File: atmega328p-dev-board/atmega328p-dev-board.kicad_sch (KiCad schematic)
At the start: 0 parts

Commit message: Completed 5V power supply schematic
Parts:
- added C1, C2: 10u, symbol Device:C_Polarized
- added C3, C4: 0.1u, symbol Device:C
- added D1: LED, symbol Device:LED
- added J2: Barrel_Jack, symbol Connector:Barrel_Jack
- added R1: 330, symbol Device:R
- added U1: LM7805_TO220, Package_TO_SOT_THT:TO-220-3_Vertical, symbol Regulator_Linear:LM7805_TO220
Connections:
- new net: C1.1, C4.1, J2.1, U1.1 (VI)
- new net: D1.2 (A), R1.2
- new net +5V: C2.1, C3.1, R1.1, U1.3 (VO)
- new net GND: C1.2, C2.2, C3.2, C4.2, D1.1 (K), J2.2, U1.2 (GND)

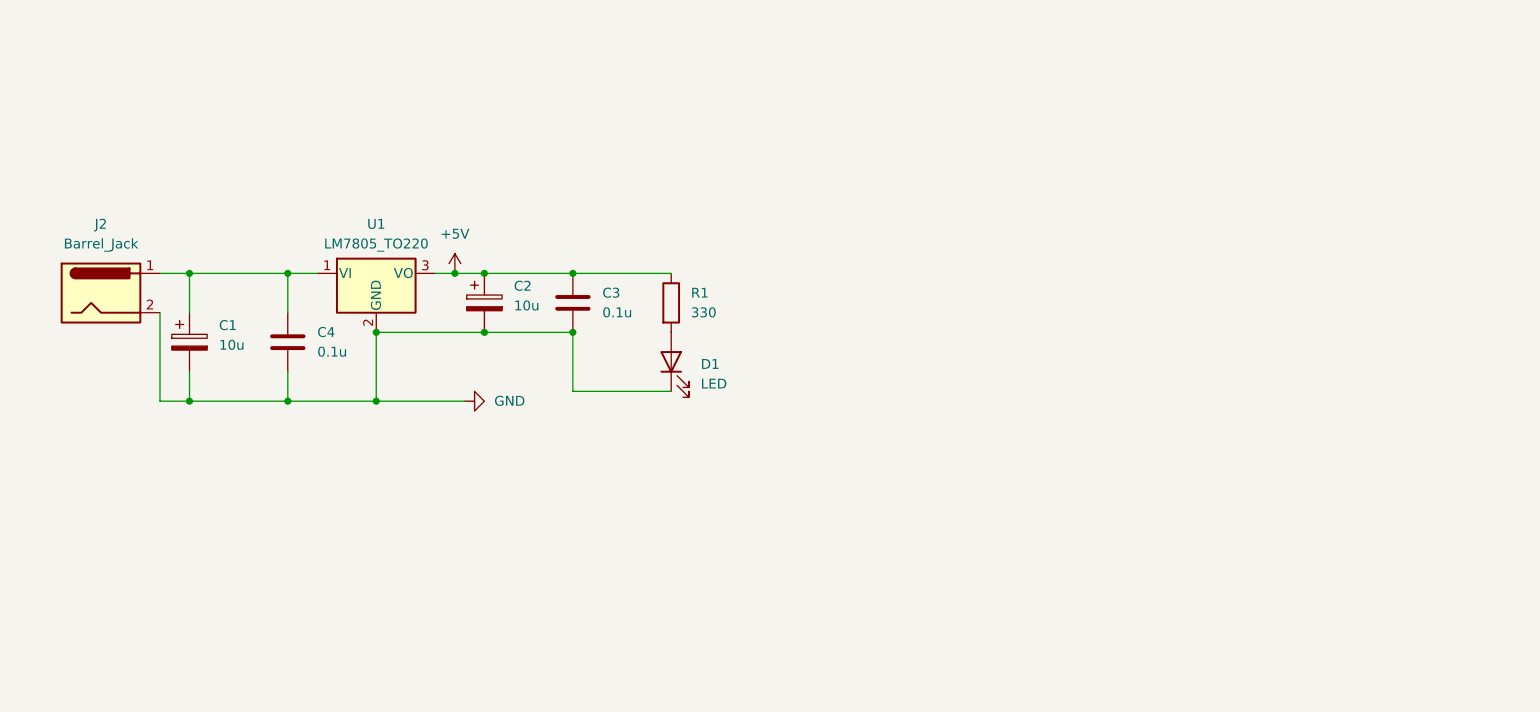
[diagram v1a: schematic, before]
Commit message: Added ATmega328P microcontroller and 16MHz crystal oscillator clock circuit
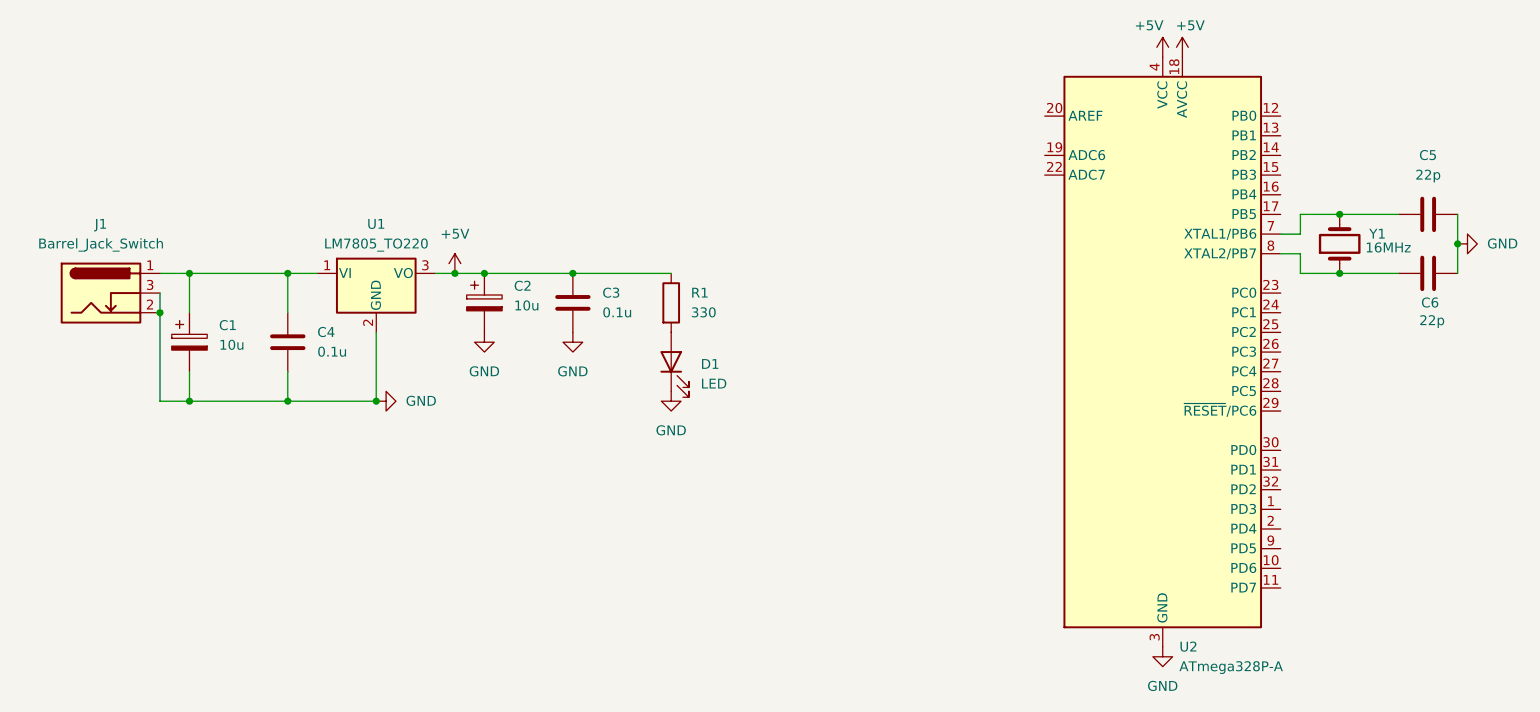
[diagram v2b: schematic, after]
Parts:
- removed J2: Barrel_Jack, symbol Connector:Barrel_Jack
- added C5, C6: 22p, symbol Device:C
- added J1: Barrel_Jack_Switch, symbol Connector:Barrel_Jack_Switch
- added U2: ATmega328P-A, Package_QFP:TQFP-32_7x7mm_P0.8mm, symbol MCU_Microchip_ATmega:ATmega328P-A
- added Y1: 16MHz, symbol Device:Crystal
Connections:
- net +5V: now also U2.18 (AVCC), U2.4 (VCC), U2.6 (VCC)
- net GND: now also C5.2, C6.2, J1.2, J1.3, U2.21 (GND), U2.3 (GND), U2.5 (GND)
- net at C1.1, C4.1, U1.1 (VI): now also J1.1
- new net: C6.1, U2.8 (XTAL2/PB7), Y1.1
- new net: C5.1, U2.7 (XTAL1/PB6), Y1.2

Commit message: Added hardware reset circuit and 6-pin ICSP programming header
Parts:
- removed U2: ATmega328P-A, Package_QFP:TQFP-32_7x7mm_P0.8mm, symbol MCU_Microchip_ATmega:ATmega328P-A
- added J2: Conn_02x03_Odd_Even, symbol Connector_Generic:Conn_02x03_Odd_Even
- added J3: Conn_01x06, symbol Connector_Generic:Conn_01x06
- added J4: Conn_01x07_Socket, symbol Connector:Conn_01x07_Socket
- added R2: 10k, symbol Device:R
- added SW1: SW_Push, symbol Switch:SW_Push
- added U3: ATmega8-16A, Package_QFP:TQFP-32_7x7mm_P0.8mm, symbol MCU_Microchip_ATmega:ATmega8-16A
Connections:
- net +5V: now also J2.2 (Pin_2), R2.2, U3.18 (AVCC), U3.4 (VCC), U3.6 (VCC)
- net GND: now also J2.6 (Pin_6), SW1.2, U3.3 (GND), U3.5 (GND)
- net at C6.1, Y1.1: now also U3.7 (PB6/XTAL1)
- net at C5.1, Y1.2: now also U3.8 (PB7/XTAL2)
- new net: J3.1 (Pin_1), U3.12 (PB0)
- new net: J3.2 (Pin_2), U3.13 (PB1)
- new net: J3.3 (Pin_3), U3.14 (PB2)
- new net: J2.4 (Pin_4), J3.4 (Pin_4), U3.15 (PB3)
- new net: J2.1 (Pin_1), J3.5 (Pin_5), U3.16 (PB4)
- new net: J2.3 (Pin_3), J3.6 (Pin_6), U3.17 (PB5)
- new net RST: J2.5 (Pin_5), R2.1, SW1.1, U3.29 (PC6/~{RESET})
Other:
- moved on the sheet: C5, C6, Y1

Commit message: Completed full schematic layout and passed ERC with zero errors
- Placed decoupling capacitors for MCU and AREF stabilizing capacitor.
- Placed breakout headers for all remaining analog and digital GPIO pins.
- Resolved power routing flags for 5V regulator.
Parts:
- removed J4: Conn_01x07_Socket, symbol Connector:Conn_01x07_Socket
- added C7, C8: 0.1u, symbol Device:C
- added J4: Conn_01x06, symbol Connector_Generic:Conn_01x06
- added J5: Conn_01x08, symbol Connector_Generic:Conn_01x08
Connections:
- net +5V: now also C8.1
- net GND: now also U3.21 (AGND), C7.1, C8.2
- net at U3.1 (PD3): now also J5.4 (Pin_4)
- net at U3.10 (PD6): now also J5.7 (Pin_7)
- net at U3.11 (PD7): now also J5.8 (Pin_8)
- net at U3.2 (PD4): now also J5.5 (Pin_5)
- net at U3.20 (AREF): now also C7.2
- net at U3.23 (PC0): now also J4.1 (Pin_1)
- net at U3.24 (PC1): now also J4.2 (Pin_2)
- net at U3.25 (PC2): now also J4.3 (Pin_3)
- net at U3.26 (PC3): now also J4.4 (Pin_4)
- net at U3.27 (PC4): now also J4.5 (Pin_5)
- net at U3.28 (PC5): now also J4.6 (Pin_6)
- net at U3.30 (PD0): now also J5.1 (Pin_1)
- net at U3.31 (PD1): now also J5.2 (Pin_2)
- net at U3.32 (PD2): now also J5.3 (Pin_3)
- net at U3.9 (PD5): now also J5.6 (Pin_6)
- no-connect marks 0 -> 2

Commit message: Imported components to PCB layout and made board boundary
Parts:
- C1, C2: footprint (none) -> Capacitor_THT:CP_Radial_D5.0mm_P2.50mm
- C3, C4, C5, C6, C7, C8: footprint (none) -> Capacitor_THT:C_Disc_D5.0mm_W2.5mm_P2.50mm
- D1: footprint (none) -> LED_THT:LED_D3.0mm
- J1: footprint (none) -> Connector_BarrelJack:BarrelJack_CUI_PJ-102AH_Horizontal
- J2: footprint (none) -> Connector_PinHeader_2.54mm:PinHeader_2x03_P2.54mm_Vertical
- J3, J4: footprint (none) -> Connector_PinHeader_2.54mm:PinHeader_1x06_P2.54mm_Vertical
- J5: footprint (none) -> Connector_PinHeader_2.54mm:PinHeader_1x08_P2.54mm_Vertical
- R1, R2: footprint (none) -> Resistor_THT:R_Axial_DIN0207_L6.3mm_D2.5mm_P10.16mm_Horizontal
- SW1: footprint (none) -> Button_Switch_THT:SW_PUSH_6mm_H5mm
- U3: footprint Package_QFP:TQFP-32_7x7mm_P0.8mm -> Package_DIP:DIP-28_W7.62mm
- Y1: footprint (none) -> Crystal:Crystal_HC49-U_Vertical
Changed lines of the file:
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@@
 			)
 		)
-		(property "Footprint" ""
+		(property "Footprint" "Capacitor_THT:C_Disc_D5.0mm_W2.5mm_P2.50mm"
 			(at 83.5152 72.39 0)
 			(hide yes)
@@
 			)
 		)
-		(property "Footprint" ""
+		(property "Footprint" "Crystal:Crystal_HC49-U_Vertical"
 			(at 176.53 68.58 0)
 			(hide yes)
@@
 			)
 		)
-		(property "Footprint" ""
+		(property "Footprint" "Capacitor_THT:C_Disc_D5.0mm_W2.5mm_P2.50mm"
 			(at 161.29 73.3552 0)
 			(hide yes)
@@
 			)
 		)
-		(property "Footprint" ""
+		(property "Footprint" "Connector_PinHeader_2.54mm:PinHeader_1x06_P2.54mm_Vertical"
 			(at 231.14 83.82 0)
 			(hide yes)
@@
 			)
 		)
-		(property "Footprint" ""
+		(property "Footprint" "Connector_PinHeader_2.54mm:PinHeader_1x06_P2.54mm_Vertical"
 			(at 231.14 66.04 0)
 			(hide yes)
@@
 		(in_pos_files yes)
 		(dnp no)
-		(fields_autoplaced yes)
 		(property "Reference" "#PWR011"
 			(at 180.34 50.8 0)
@@
 			)
 		)
-		(property "Footprint" ""
+		(property "Footprint" "Resistor_THT:R_Axial_DIN0207_L6.3mm_D2.5mm_P10.16mm_Horizontal"
 			(at 182.118 50.8 90)
 			(hide yes)
@@
 			)
 		)
-		(property "Footprint" ""
+		(property "Footprint" "Connector_PinHeader_2.54mm:PinHeader_1x08_P2.54mm_Vertical"
 			(at 231.14 104.14 0)
 			(hide yes)
@@
 			)
 		)
-		(property "Footprint" ""
+		(property "Footprint" "Capacitor_THT:C_Disc_D5.0mm_W2.5mm_P2.50mm"
 			(at 198.4248 39.37 0)
 			(hide yes)
@@
 			)
 		)
-		(property "Footprint" ""
+		(property "Footprint" "Connector_PinHeader_2.54mm:PinHeader_2x03_P2.54mm_Vertical"
 			(at 234.95 41.91 0)
 			(hide yes)
@@
 			)
 		)
-		(property "Footprint" ""
+		(property "Footprint" "Connector_BarrelJack:BarrelJack_CUI_PJ-102AH_Horizontal"
 			(at 59.69 63.246 0)
 			(hide yes)
@@
 			)
 		)
-		(property "Footprint" ""
+		(property "Footprint" "Capacitor_THT:CP_Radial_D5.0mm_P2.50mm"
 			(at 108.9152 67.31 0)
 			(hide yes)
@@
 			)
 		)
-		(property "Footprint" ""
+		(property "Footprint" "Capacitor_THT:CP_Radial_D5.0mm_P2.50mm"
 			(at 70.8152 72.39 0)
 			(hide yes)
@@
 			)
 		)
-		(property "Footprint" ""
+		(property "Footprint" "Capacitor_THT:C_Disc_D5.0mm_W2.5mm_P2.50mm"
 			(at 181.61 77.7748 0)
 			(hide yes)
@@
 			)
 		)
-		(property "Footprint" ""
+		(property "Footprint" "Button_Switch_THT:SW_PUSH_6mm_H5mm"
 			(at 170.18 59.69 0)
 			(hide yes)
@@
 			)
 		)
-		(property "Footprint" ""
+		(property "Footprint" "Resistor_THT:R_Axial_DIN0207_L6.3mm_D2.5mm_P10.16mm_Horizontal"
 			(at 130.302 63.5 90)
 			(hide yes)
@@
 			)
 		)
-		(property "Footprint" "Package_QFP:TQFP-32_7x7mm_P0.8mm"
+		(property "Footprint" "Package_DIP:DIP-28_W7.62mm"
 			(at 199.39 88.9 0)
 			(hide yes)
@@
 			)
 		)
-		(property "Footprint" ""
+		(property "Footprint" "Capacitor_THT:C_Disc_D5.0mm_W2.5mm_P2.50mm"
 			(at 120.3452 67.31 0)
 			(hide yes)
@@
 			)
 		)
-		(property "Footprint" ""
+		(property "Footprint" "Capacitor_THT:C_Disc_D5.0mm_W2.5mm_P2.50mm"
 			(at 161.29 65.7352 0)
 			(hide yes)
@@
 			)
 		)
-		(property "Footprint" ""
+		(property "Footprint" "LED_THT:LED_D3.0mm"
 			(at 132.08 71.12 0)
 			(hide yes)
